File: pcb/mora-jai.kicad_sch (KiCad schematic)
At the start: 25 parts, among them J1 Conn_01x02, J2 Conn_01x04, J3 Conn_01x02, SW1 SW_Push, SW10 SW_Push, SW11 SW_Push, SW12 SW_Push, SW13 SW_Push, SW14 SW_Push, SW15 SW_Push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

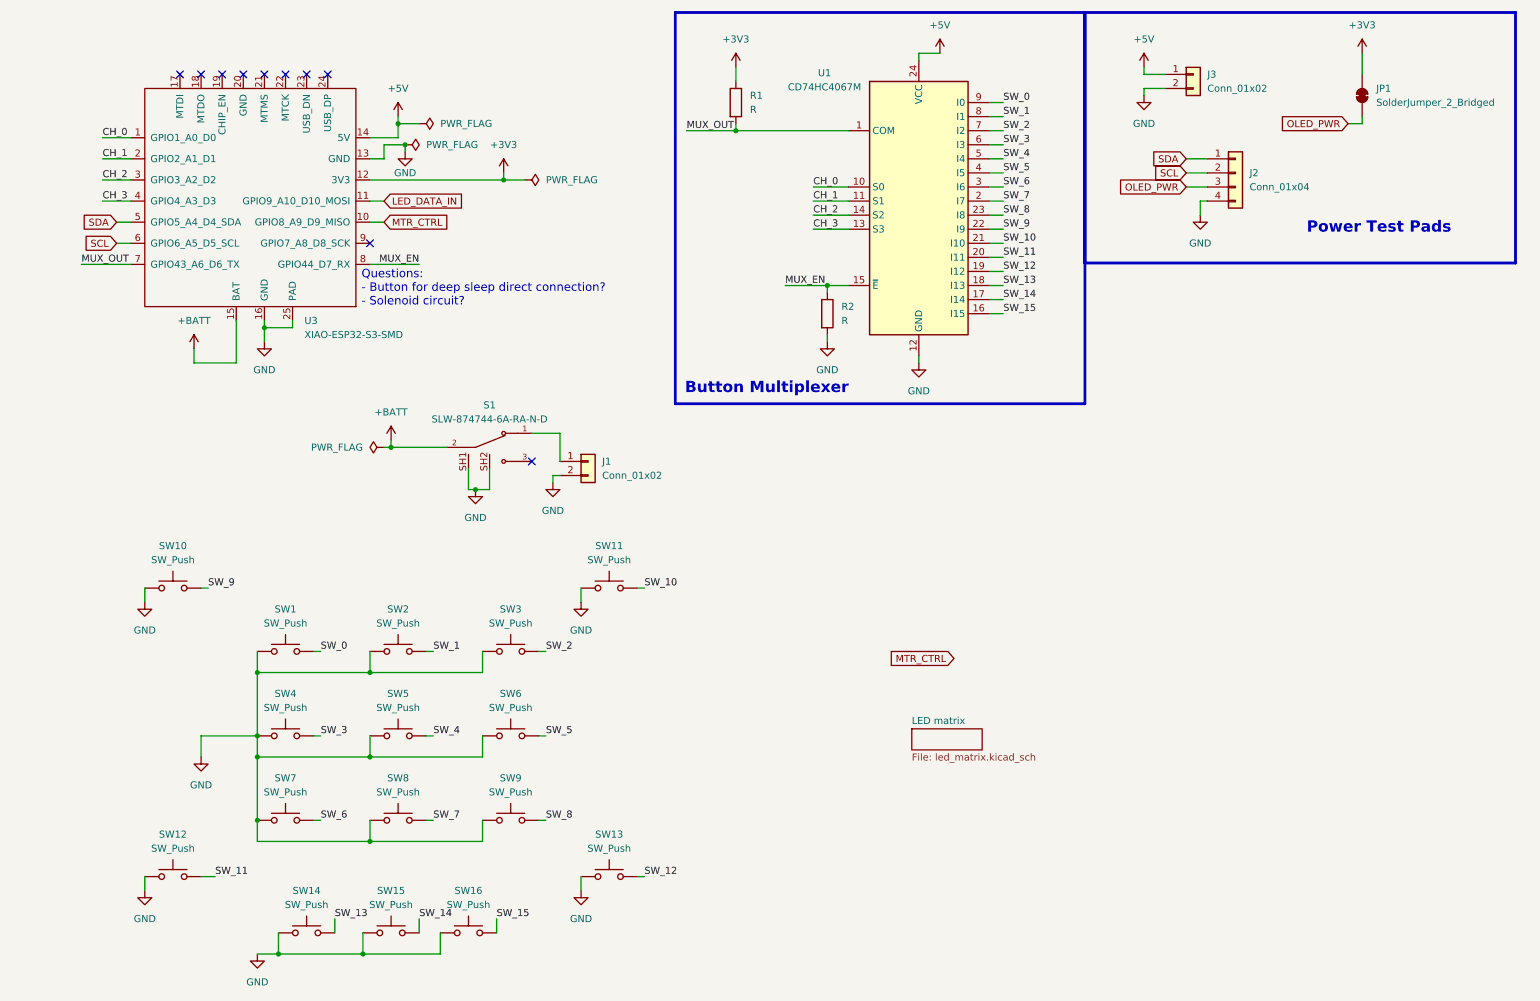
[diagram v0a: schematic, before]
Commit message: proof of concept for solenoid circuit
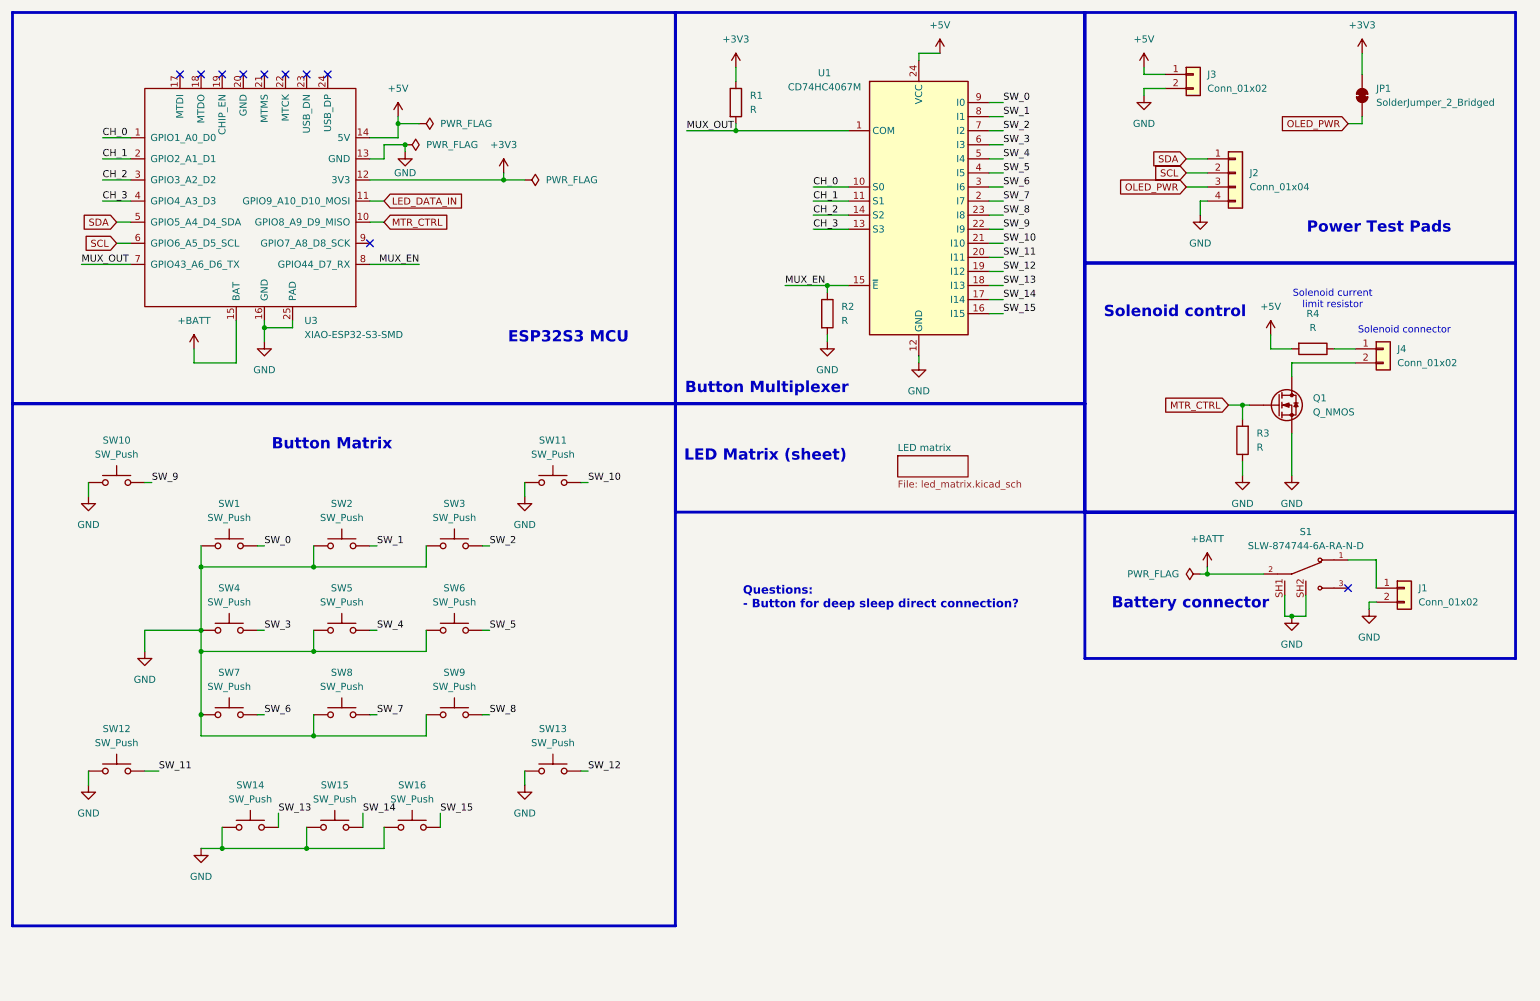
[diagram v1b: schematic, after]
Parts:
- added J4: Conn_01x02, Connector_JST:JST_PH_S2B-PH-K_1x02_P2.00mm_Horizontal, symbol Connector_Generic:Conn_01x02
- added Q1: Q_NMOS, symbol Device:Q_NMOS
- added R3, R4: R, symbol Device:R
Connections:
- net +5V: now also R4.2
- net GND: now also Q1.S, R3.1
- net MTR_CTRL: now also Q1.G, R3.2
- new net: J4.2 (Pin_2), Q1.D
- new net: J4.1 (Pin_1), R4.1
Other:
- note added: "Battery connector"
- note added: "Button Matrix"
- note added: "ESP32S3 MCU"
- note added: "LED Matrix (sheet)"
- note added: "Questions: - Button for deep sleep direct connection?"
- note added: "Solenoid connector"
- note added: "Solenoid control"
- note added: "Solenoid current limit resistor"
- note removed: "Questions: - Button for deep sleep direct connection? - Solenoid circuit?"
- moved on the sheet: J1, S1, SW1, SW10, SW11, SW12, SW13, SW14, SW15, SW16, SW2, SW3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

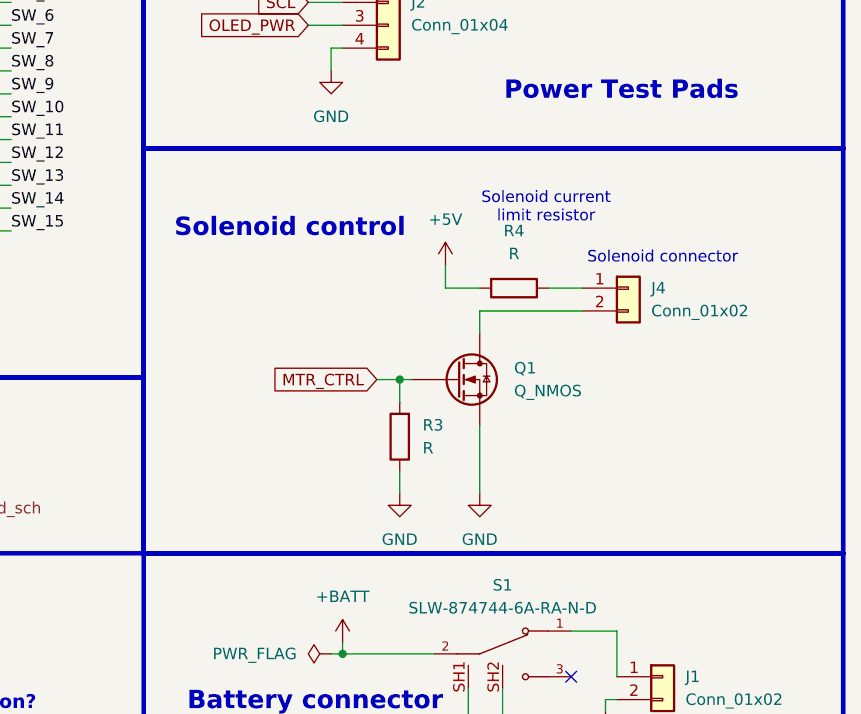
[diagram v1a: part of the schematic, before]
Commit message: update motor control circuit in schematic
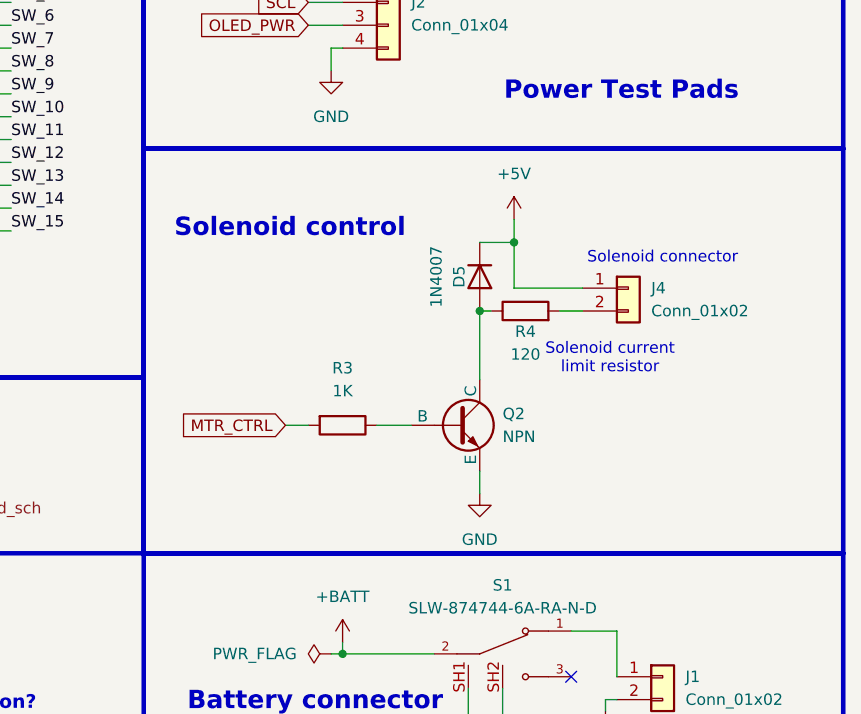
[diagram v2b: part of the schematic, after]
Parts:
- removed Q1: Q_NMOS, symbol Device:Q_NMOS
- added D5: 1N4007, Diode_THT:D_DO-41_SOD81_P10.16mm_Horizontal, symbol Diode:1N4007
- added Q2: NPN, symbol Simulation_SPICE:NPN
- R3: value R -> 1K
- R4: value R -> 120
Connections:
- net +5V: now also J4.1 (Pin_1), D5.1 (K); no longer R4.2
- net GND: now also Q2.3 (E); no longer R3.1
- net at J4.2 (Pin_2): now also R4.2
- net at R4.1: now also D5.2 (A), Q2.1 (C); no longer J4.1 (Pin_1)
- new net: Q2.2 (B), R3.1
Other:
- moved on the sheet: R3, R4

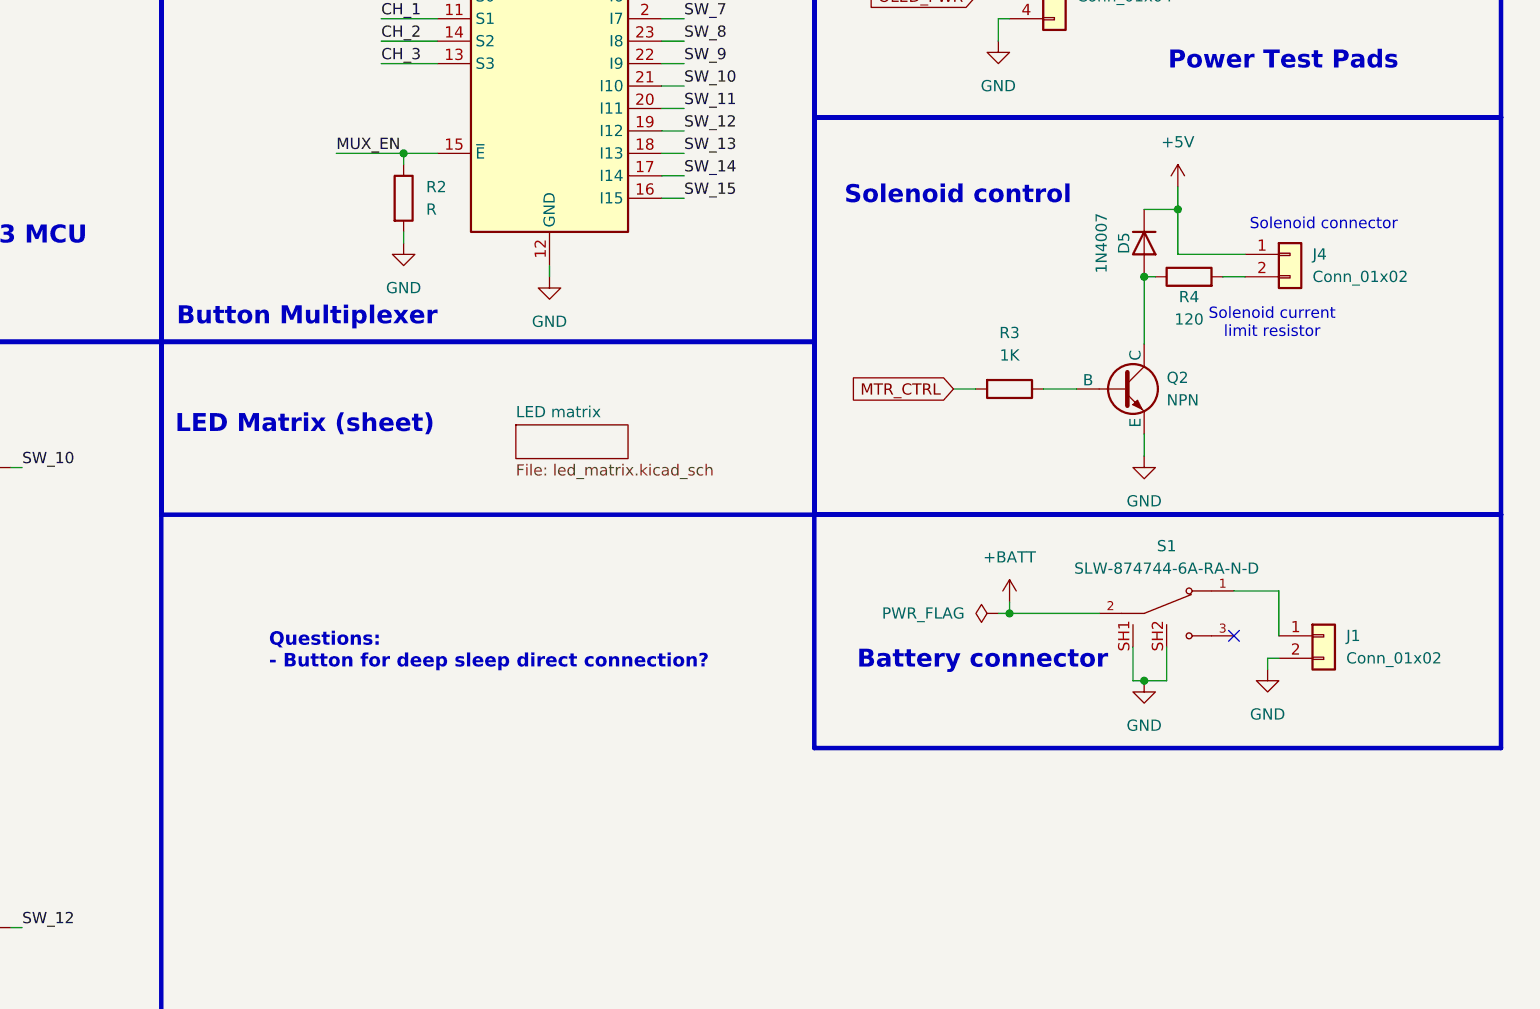
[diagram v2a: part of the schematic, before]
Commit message: add servo control circuit to PCB
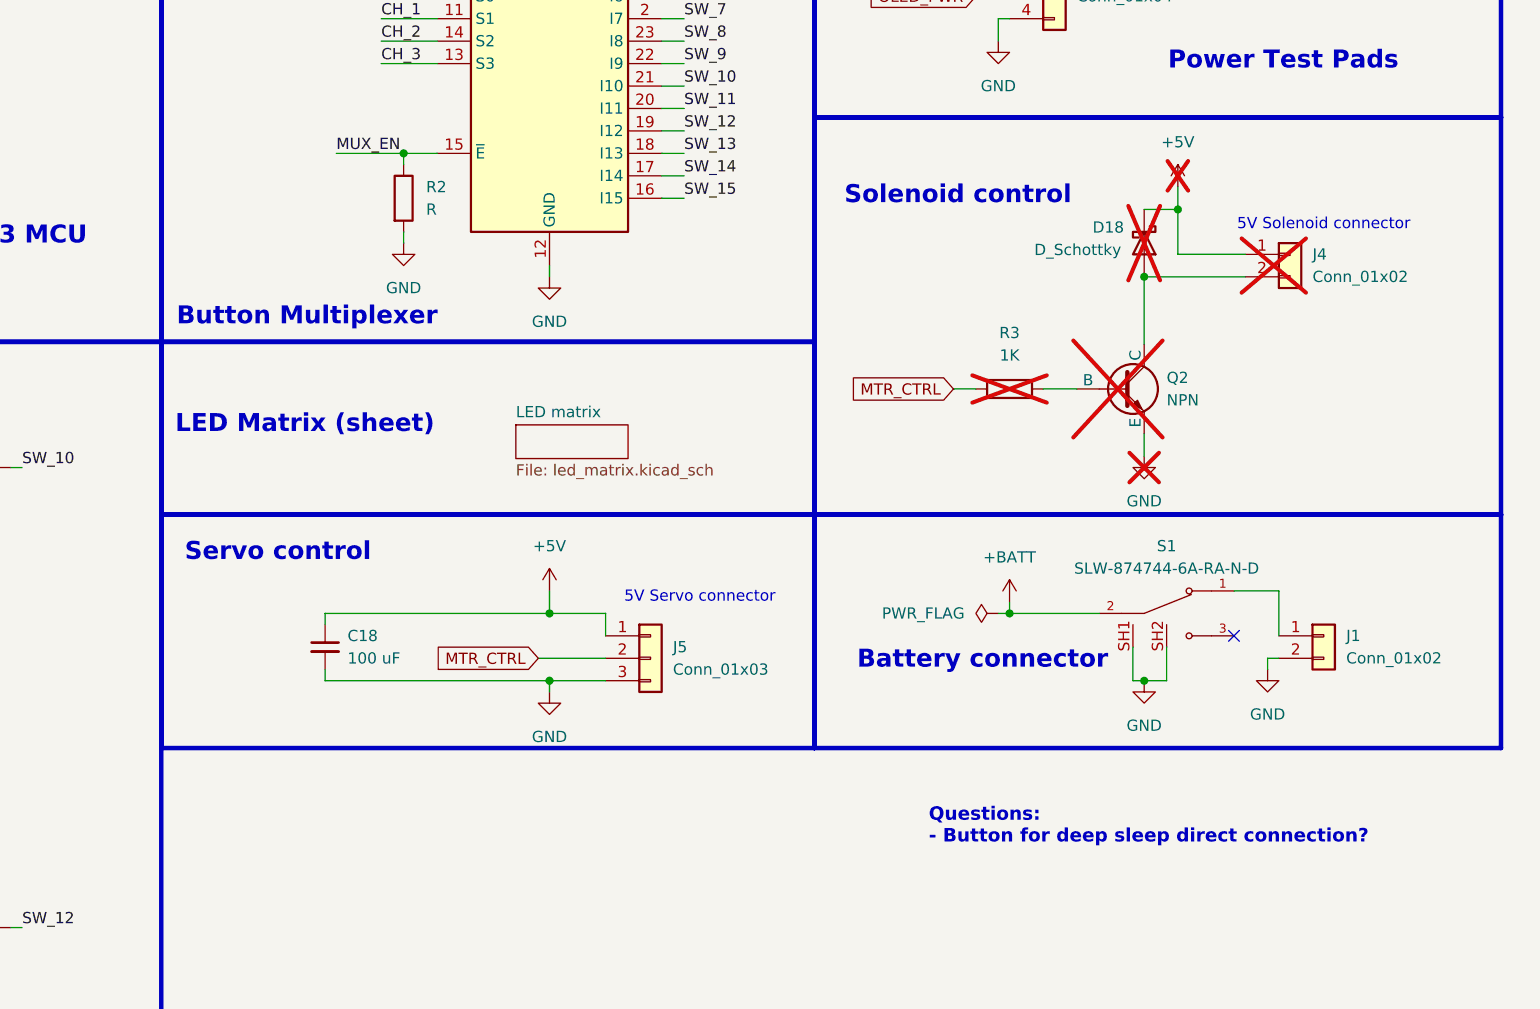
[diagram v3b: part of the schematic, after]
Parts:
- removed D5: 1N4007, Diode_THT:D_DO-41_SOD81_P10.16mm_Horizontal, symbol Diode:1N4007
- removed R4: 120, symbol Device:R
- added C18: 100 uF, symbol Device:C_Small
- added D18: D_Schottky, symbol Device:D_Schottky
- added J5: Conn_01x03, Connector_PinHeader_2.54mm:PinHeader_1x03_P2.54mm_Vertical, symbol Connector_Generic:Conn_01x03
- J4, Q2, R3: now not fitted; now left out of the parts list
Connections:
- net +5V: now also C18.1, D18.1 (K), J5.1 (Pin_1)
- net GND: now also C18.2, J5.3 (Pin_3)
- net MTR_CTRL: now also J5.2 (Pin_2)
- net at Q2.1 (C): now also J4.2 (Pin_2), D18.2 (A)
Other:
- note added: "5V Servo connector"
- note added: "5V Solenoid connector"
- note added: "Servo control"
- note removed: "Solenoid connector"
- note removed: "Solenoid current limit resistor"
